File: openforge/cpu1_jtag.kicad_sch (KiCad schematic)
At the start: 46 parts, among them P2 Heaader 2x10 1.27mm, U16 74LVC1G07, U3 74LVC1G06, U5 AM3352BZCZ100, U6 SN74LVC1G74DCTR, Y1 32.768K/12.5p, Y2 24MHz/20p, Y4 ASCO

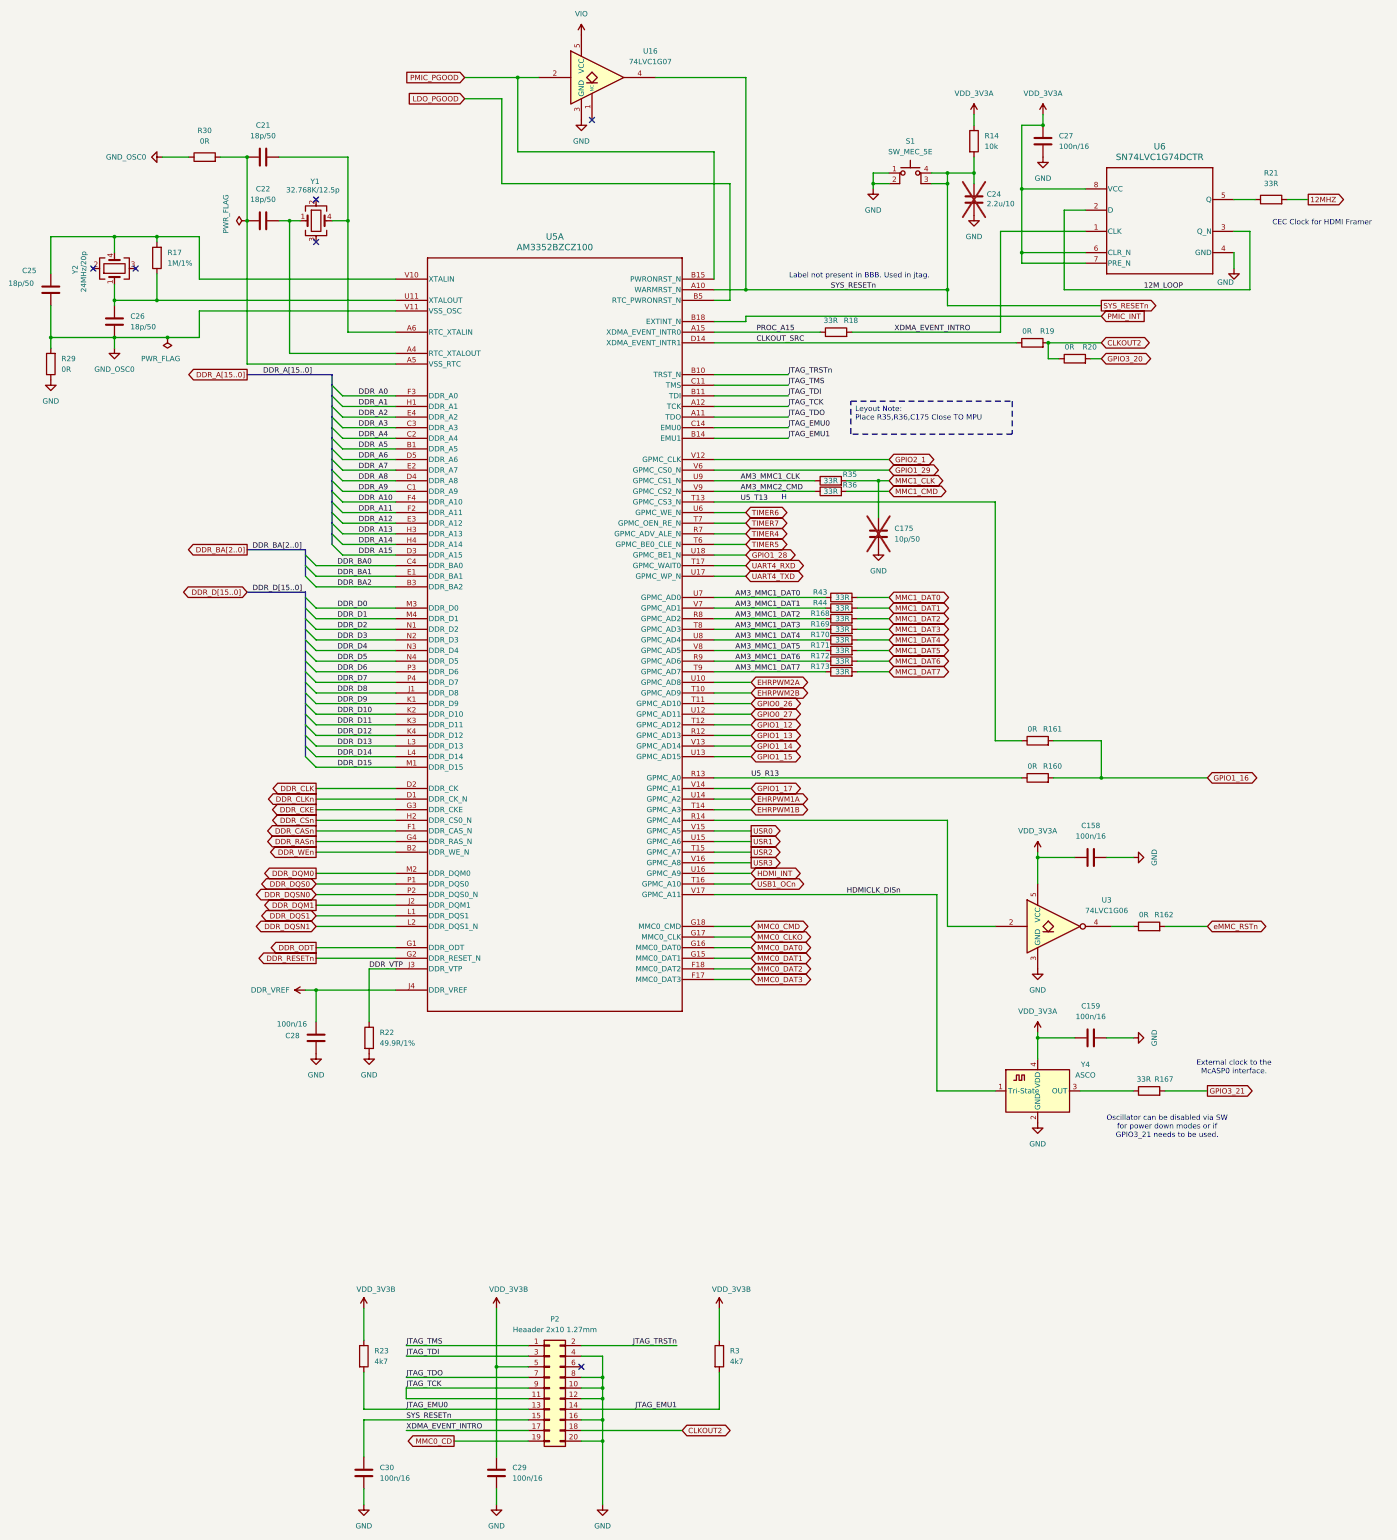
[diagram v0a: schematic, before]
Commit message: added footprint associations
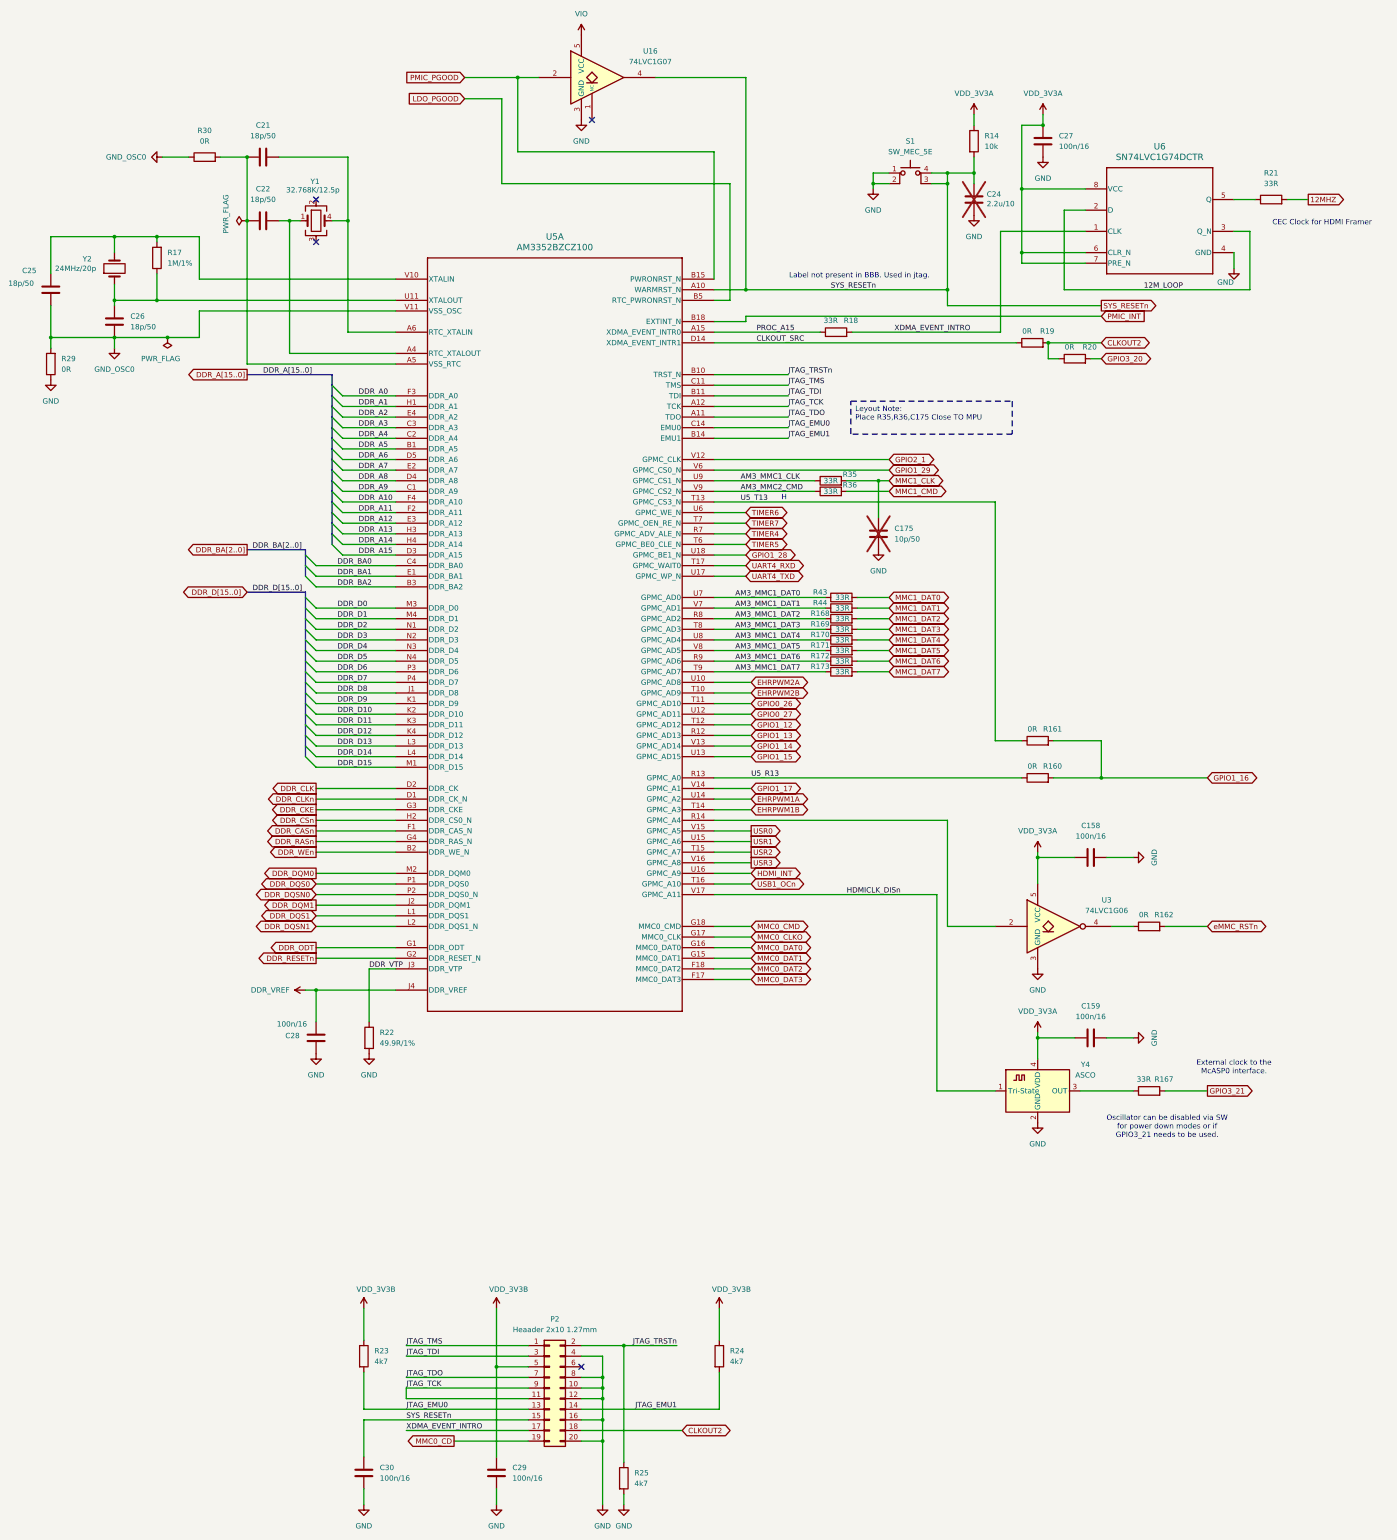
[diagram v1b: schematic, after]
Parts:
- removed Y2: 24MHz/20p, symbol MT41K256M16TW-107_P:Crystal_GND23
- added R25: 4k7, Resistor_SMD:R_0402_1005Metric, symbol MT41K256M16TW-107_P:R
- added Y2: 24MHz/20p, Crystal:Crystal_SMD_Abracon_ABM7-2Pin_6.0x3.5mm, symbol MT41K256M16TW-107_P:Crystal
- R14, R160, R161, R162, R167, R168, R169, R17, R170, R171, R172, R173, R18, R19, R20, R21, R22, R23, R29, R30, R35, R36, R43, R44: footprint (none) -> Resistor_SMD:R_0402_1005Metric
- R24: renamed from R3; footprint (none) -> Resistor_SMD:R_0402_1005Metric
- S1: footprint (none) -> footprints:KMR2xxG_CNK
- U16, U3: footprint (none) -> footprints:DCK0005A_L
- U5: footprint (none) -> footprints:ZCZ0324A
- U6: footprint (none) -> footprints:DCT0008A_L
- Y1: footprint (none) -> Crystal:Crystal_SMD_5032-4Pin_5.0x3.2mm
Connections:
- net GND: now also R25.2
- net JTAG_TRSTn: now also R25.1
- net at C26.2, R17.1, U5.U11 (XTALOUT): now also Y2.1
- net at C25.2, R17.2, U5.V10 (XTALIN): now also Y2.2
- no-connect marks 6 -> 4

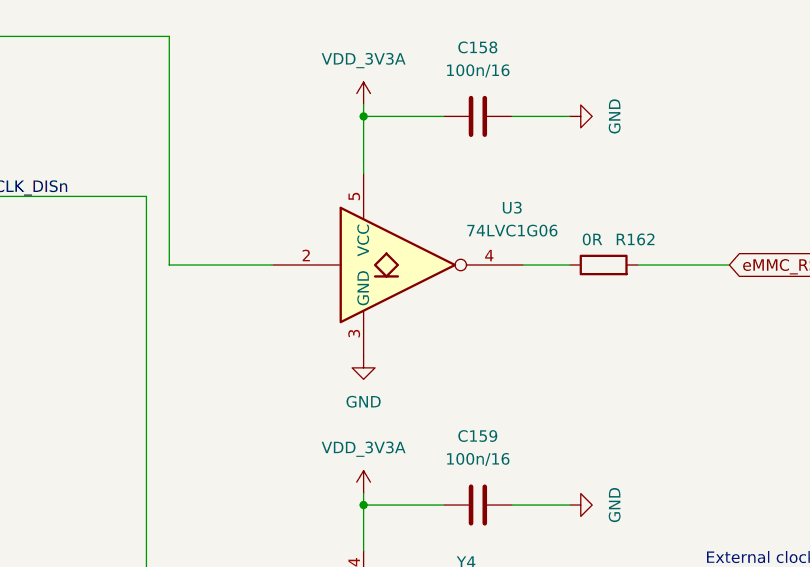
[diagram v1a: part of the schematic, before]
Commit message: Completed footprint association. Partially placed top side components on PCB
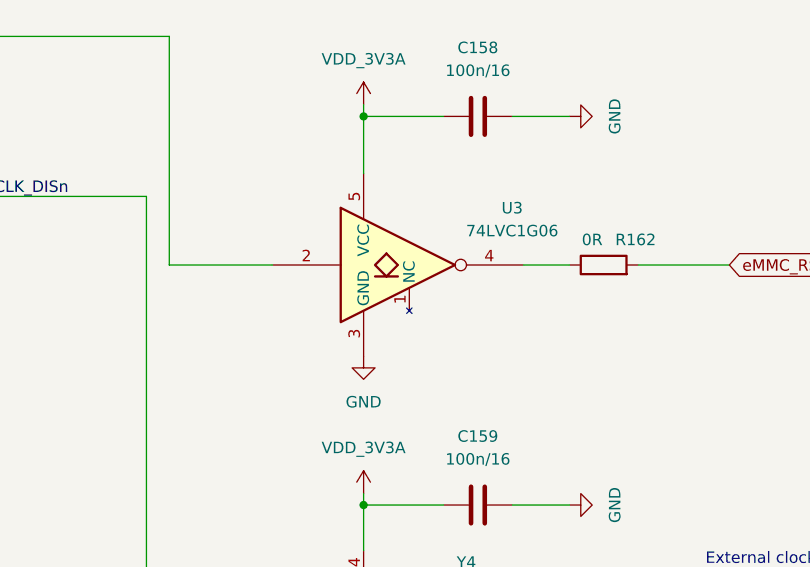
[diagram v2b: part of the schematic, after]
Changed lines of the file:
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@@
 		(pin "5"
+		)
+		(pin "1"
 		)
 		(instances

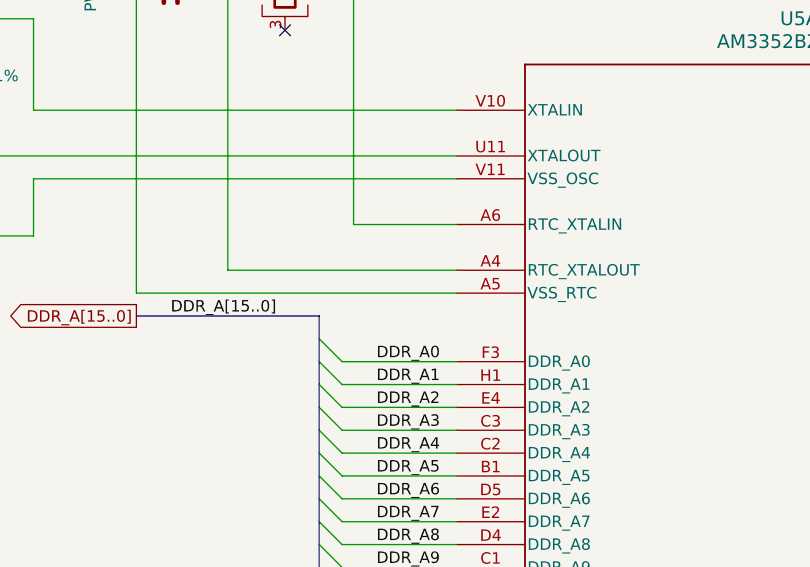
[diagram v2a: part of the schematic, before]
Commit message: PCB all layers copied from beaglebone black
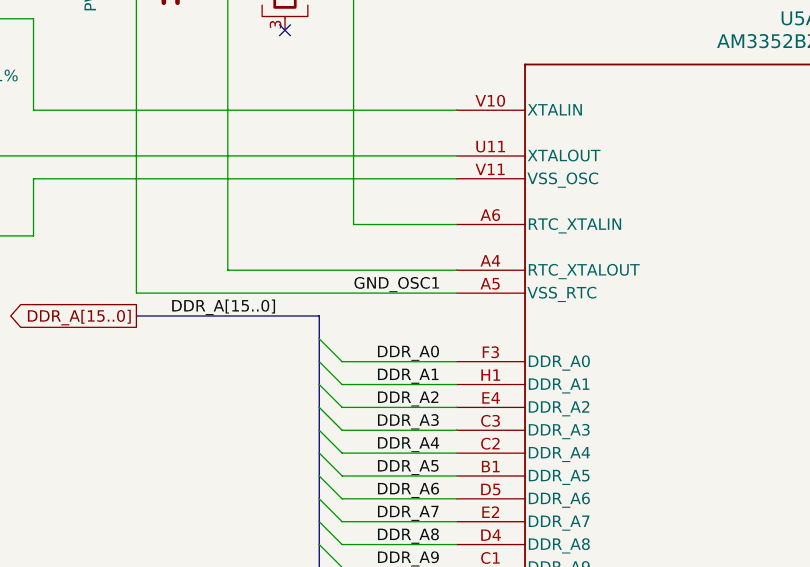
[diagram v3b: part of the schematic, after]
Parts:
- P2: footprint Connector_PinHeader_1.27mm:PinHeader_2x10_P1.27mm_Vertical_SMD -> footprints:header-10x2-1.27
- U6: footprint footprints:DCT0008A_L -> footprints:DCT8
- Y1: footprint Crystal:Crystal_SMD_5032-4Pin_5.0x3.2mm -> Crystal:Crystal_SMD_7050-4Pin_7.0x5.0mm
- Y4: footprint Oscillator:Oscillator_SMD_Abracon_ASCO-4Pin_1.6x1.2mm -> Oscillator:Oscillator_SMD_Abracon_ASDMB-4Pin_2.5x2.0mm
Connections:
- net GND_OSC1: now reaches C21.1, C22.1, R30.2, U5.A5 (VSS_RTC)
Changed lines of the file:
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@@
 		)
 	)
+	(label "GND_OSC1"
+		(at 208.28 107.95 0)
+		(fields_autoplaced yes)
+		(effects
+			(font
+				(size 1.27 1.27)
+			)
+			(justify left bottom)
+		)
+	)
 	(label "DDR_A2"
 		(at 210.82 120.65 0)
@@
 			)
 		)
-		(property "Footprint" "Crystal:Crystal_SMD_5032-4Pin_5.0x3.2mm"
+		(property "Footprint" "Crystal:Crystal_SMD_7050-4Pin_7.0x5.0mm"
 			(at 200.66 73.66 0)
 			(effects
@@
 			)
 		)
-		(property "Footprint" "Connector_PinHeader_1.27mm:PinHeader_2x10_P1.27mm_Vertical_SMD"
+		(property "Footprint" "footprints:header-10x2-1.27"
 			(at 256.54 353.06 0)
 			(effects
@@
 			)
 		)
-		(property "Footprint" "footprints:DCT0008A_L"
+		(property "Footprint" "footprints:DCT8"
 			(at 402.59 73.66 0)
 			(effects
@@
 			)
 		)
-		(property "Footprint" "Oscillator:Oscillator_SMD_Abracon_ASCO-4Pin_1.6x1.2mm"
+		(property "Footprint" "Oscillator:Oscillator_SMD_Abracon_ASDMB-4Pin_2.5x2.0mm"
 			(at 375.92 290.83 0)
 			(effects
